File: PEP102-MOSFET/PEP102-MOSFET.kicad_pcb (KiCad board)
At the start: 2 copper layers, 45 x 45 mm, 15 parts, among them J1 Screw_Terminal_01x02, J2 Screw_Terminal_01x02, J3 Screw_Terminal_01x02, Q19 2N7002

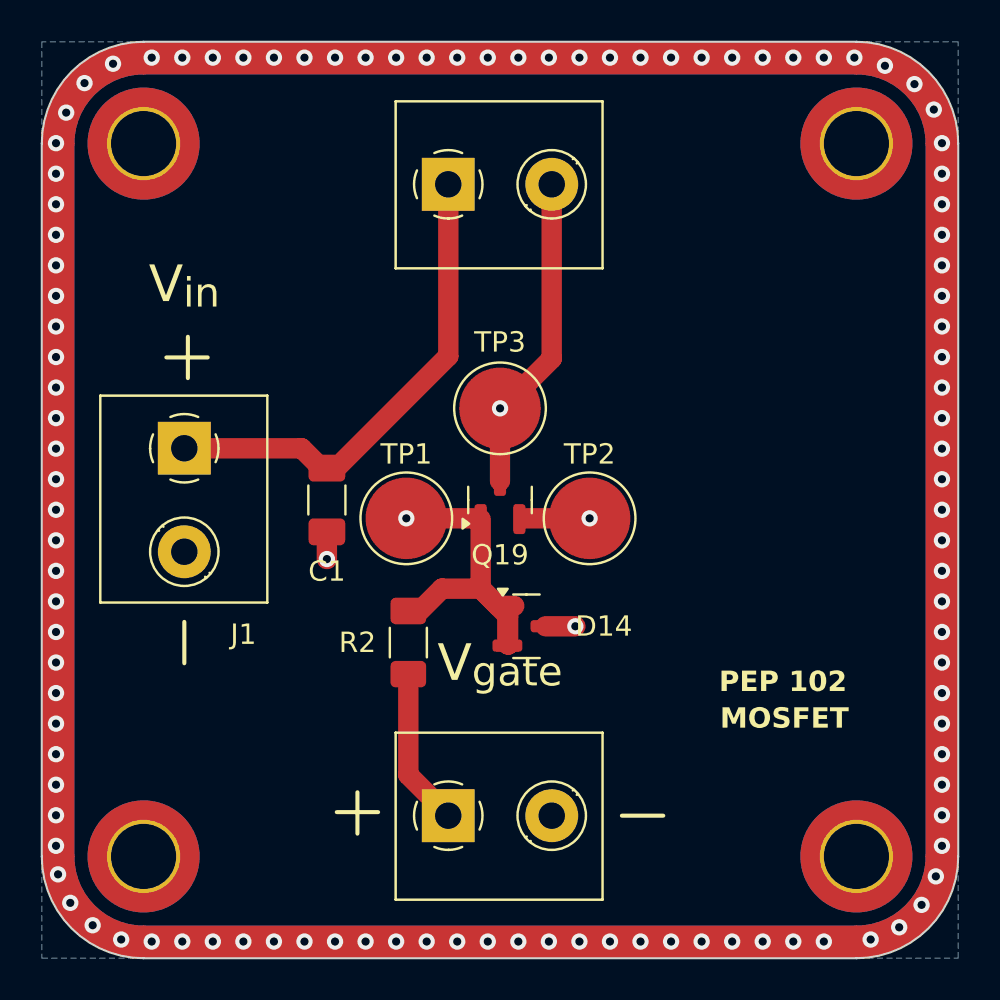
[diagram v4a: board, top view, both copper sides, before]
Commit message: MOSFET updated.
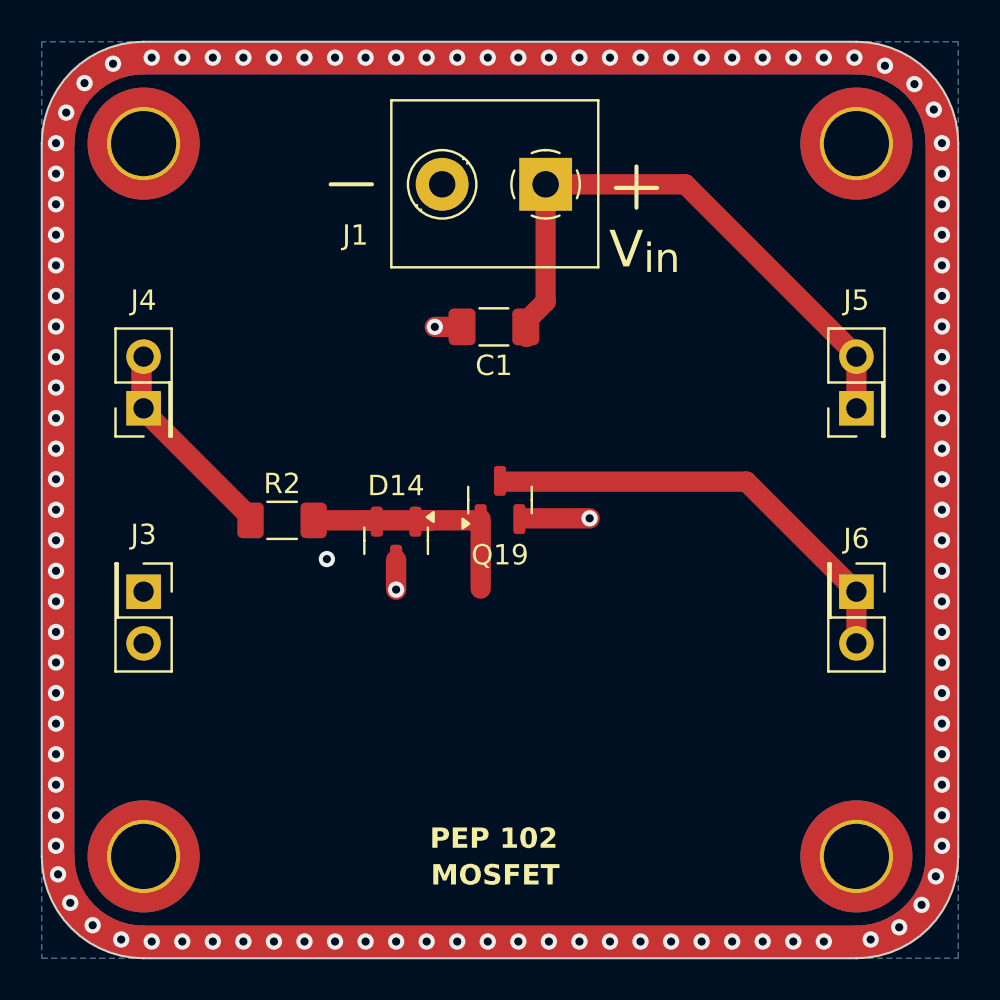
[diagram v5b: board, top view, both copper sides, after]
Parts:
- removed ?: , clipboard:cd909e86-6193-4077-a0b5-245ea85f982c
- removed the J3 at (122.5, 138.0)
- removed TP1, TP2, TP3: TestPoint, TestPoint:TestPoint_Pad_D4.0mm
- added J4: Conn_01x02_Pin, Connector_PinHeader_2.54mm:PinHeader_2x01_P2.54mm_Vertical, F.Cu at (105.0, 118.0)
- added J5: Conn_01x02_Pin, Connector_PinHeader_2.54mm:PinHeader_2x01_P2.54mm_Vertical, F.Cu at (140.0, 118.0)
- added J6: Conn_01x02_Pin, Connector_PinHeader_2.54mm:PinHeader_2x01_P2.54mm_Vertical, F.Cu at (140.0, 127.0)
- J3: renamed from J2; value Screw_Terminal_01x02 -> Conn_01x02_Pin; footprint PEP_library:Screw terminal -> Connector_PinHeader_2.54mm:PinHeader_2x01_P2.54mm_Vertical
- moved J3 26.6 mm to (105.0, 127.0), turned to -90 degrees
- moved J1 21.7 mm to (122.2, 107.0), turned to 180 degrees
- moved C1 11.8 mm to (122.2, 114.0), turned to 180 degrees
- moved R2 8.63 mm to (111.8, 123.5), turned to 0 degrees
- moved D14 7.66 mm to (117.4, 124.5), turned to -90 degrees
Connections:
- J3 pad 1: VCC -> 0
- J3 pad 2: Net-(J2-Pin_2) -> 0
- Q19 pad 3: Net-(J2-Pin_2) -> Net-(J6-Pin_1)
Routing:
- net Net-(J6-Pin_1): track 0.00 -> 22.2 mm
- net Net-(J2-Pin_2): track 15.7 -> 0.00 mm, vias 1 -> 0
- net VCC: track 24.2 -> 29.4 mm
- net Net-(Q19-G): track 17.5 -> 12.8 mm, vias 1 -> 0
- net NMOS_GATE: track 7.19 -> 10.4 mm
- net 0: vias 112 -> 113

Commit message: Nova estetika.
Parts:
- added C1: 100n, Capacitor_SMD:C_1206_3216Metric_Pad1.33x1.80mm_HandSolder, F.Cu at (122.3, 114.0)
- added REF**: R_silk_symbol, PEP_library:R_silk_symbol, F.Cu at (110.0, 116.7)
- added REF**: zener_silk, PEP_library:zener_silk, F.Cu at (122.3, 133.4)
- added REF**: C_silk_symbol, PEP_library:C_silk_symbol, F.Cu at (125.3, 118.8)
- added REF**: NMOS_silk, PEP_library:NMOS_silk, F.Cu at (123.8, 131.4)
- added REF**: zener_silk, PEP_library:zener_silk, F.Cu at (119.3, 133.4)
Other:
- board text added: "Q2"
- board text removed: "V_{drain}"
